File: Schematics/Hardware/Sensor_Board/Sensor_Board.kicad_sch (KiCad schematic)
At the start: 86 parts, among them J1 Conn_02x13_Odd_Even, J2 Conn_02x20_Odd_Even

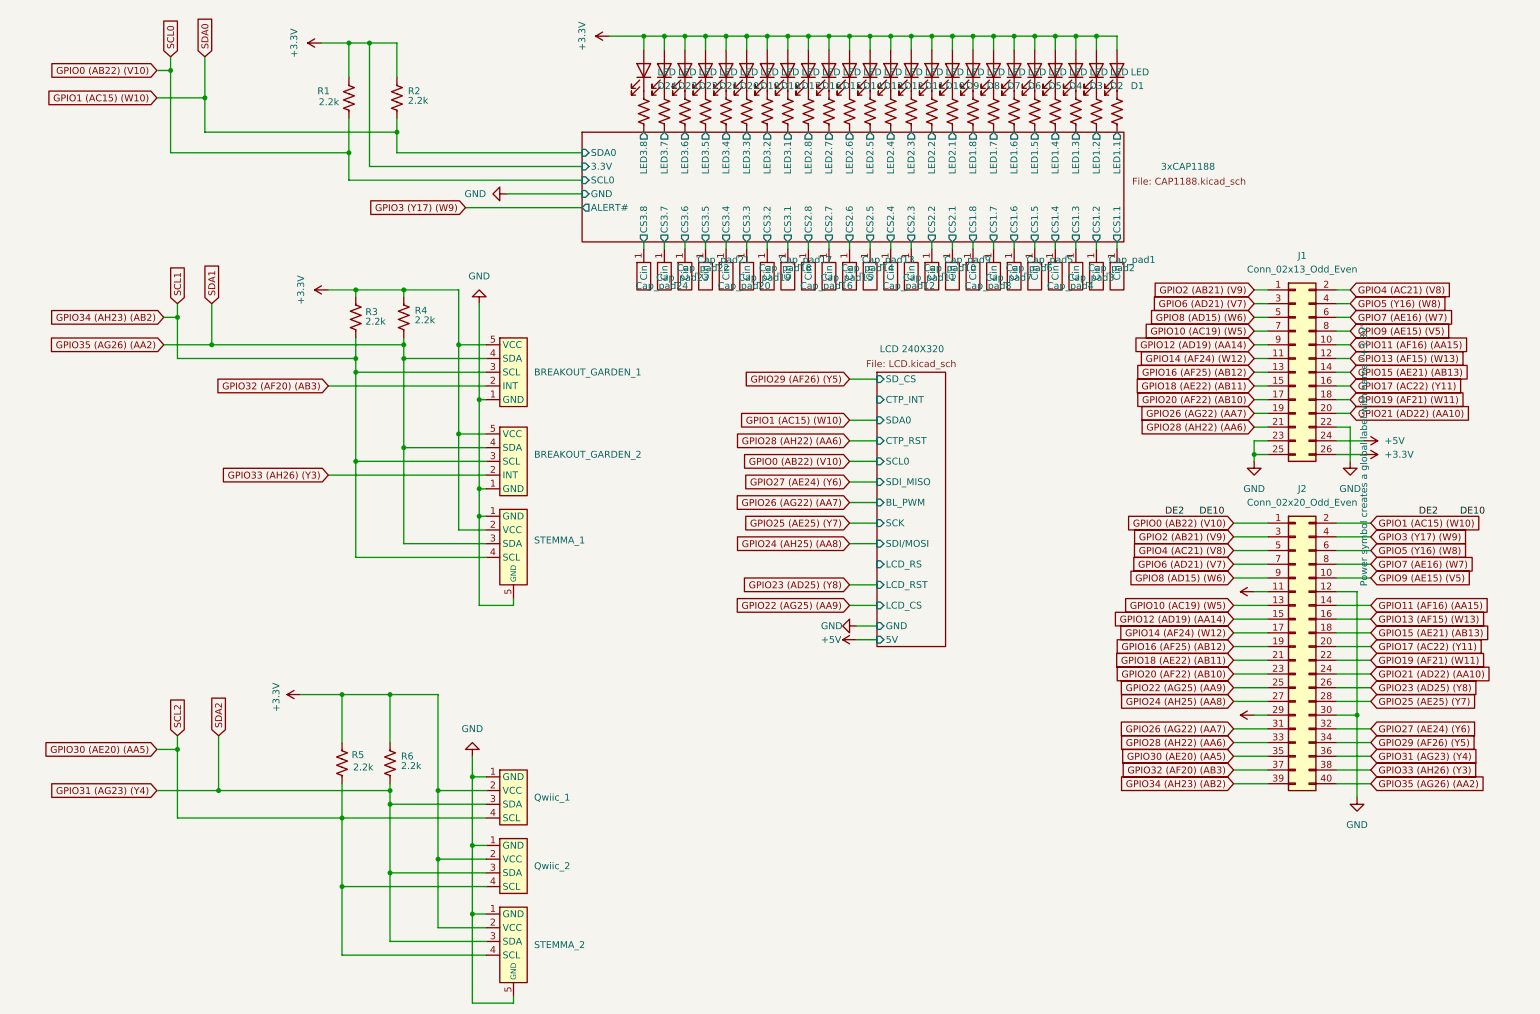
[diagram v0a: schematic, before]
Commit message: Updated Sensor board schematic/PCB
Still need to double check STEMMA connector and LCD standoff placement.
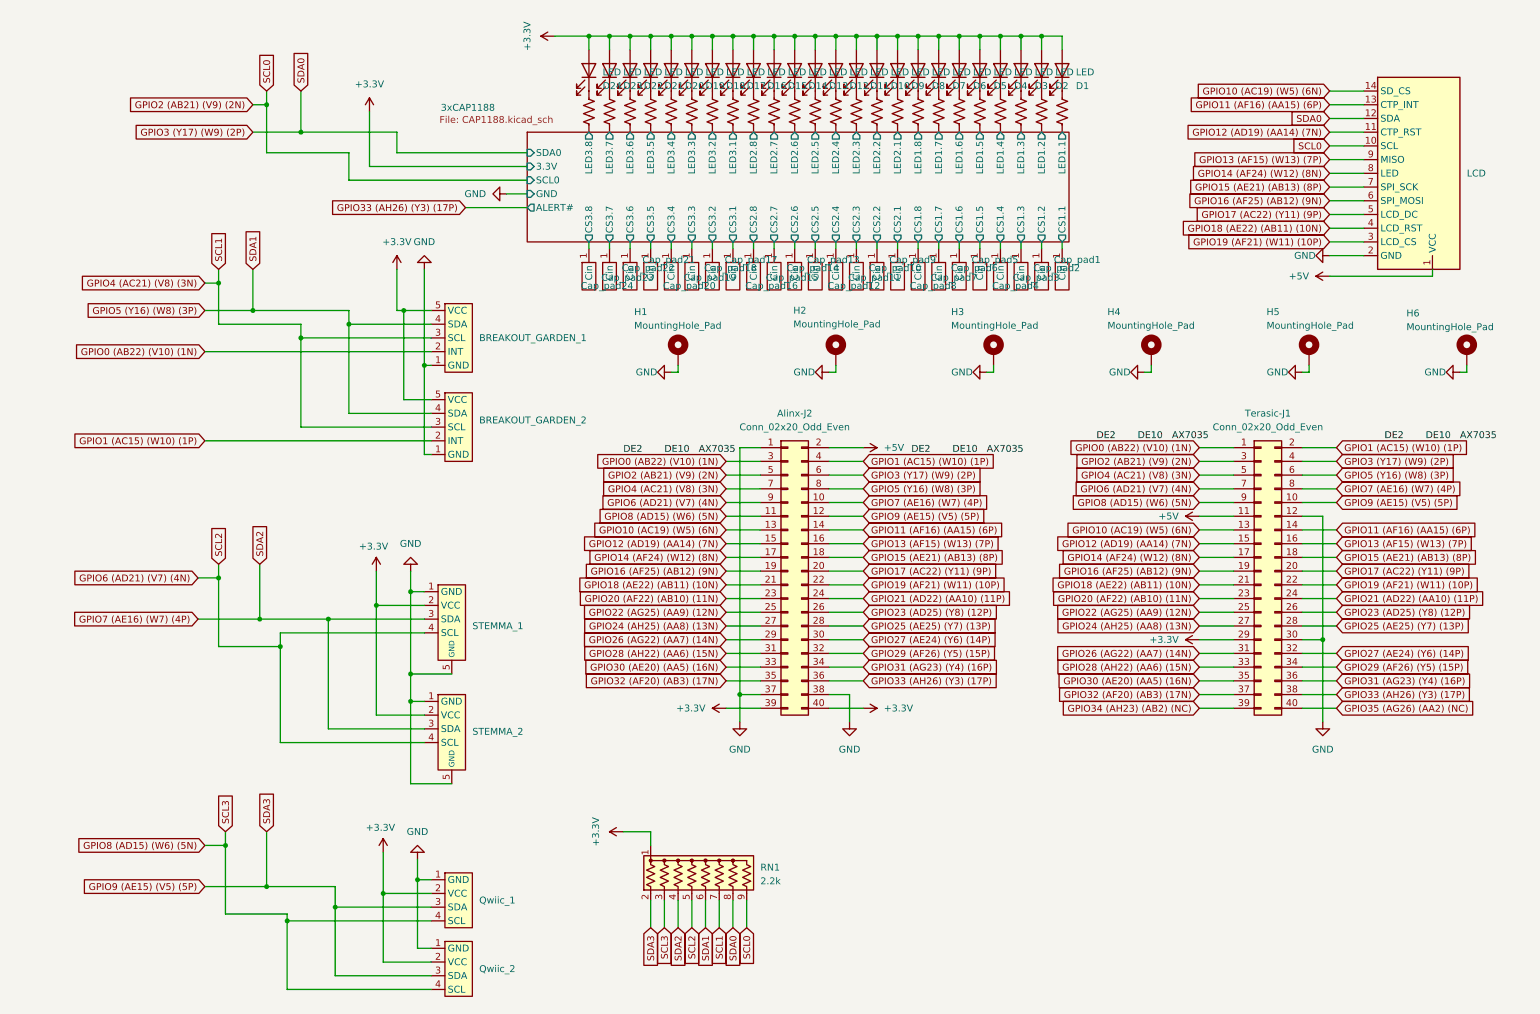
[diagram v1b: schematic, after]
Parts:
- removed J1: Conn_02x13_Odd_Even, Connector_PinHeader_2.54mm:PinHeader_2x13_P2.54mm_Vertical, symbol Connector_Generic:Conn_02x13_Odd_Even
- removed R1, R2, R3, R4, R5, R6: 2.2k, Resistor_THT:R_Axial_DIN0207_L6.3mm_D2.5mm_P10.16mm_Horizontal, symbol Device:R_US
- added Alinx-J2: Conn_02x20_Odd_Even, Connector_IDC:IDC-Header_2x20_P2.54mm_Vertical, symbol Connector_Generic:Conn_02x20_Odd_Even
- added H1, H2, H3, H4, H5, H6: MountingHole_Pad, MountingHole:MountingHole_2.5mm_Pad_Via, symbol Mechanical:MountingHole_Pad
- added RN1: 2.2k, Resistor_THT:R_Array_SIP9, symbol Device:R_Network08_US
- added U5: LCD, Connector_PinSocket_2.54mm:PinSocket_1x14_P2.54mm_Vertical, symbol Symbols:LCD240X320
- D1, D10, D11, D12, D13, D14, D15, D16, D17, D18, D19, D2, D20, D21, D22, D23, D24, D3, D4, D5, D6, D7, D8, D9: footprint LED_THT:LED_D3.0mm -> Diode_SMD:D_0805_2012Metric
- renumbered J2 to Terasic-J1
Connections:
- net GPIO4 (AC21) (V8) is gone; now on net GPIO4 (AC21) (V8) (3N): Terasic-J1.5 (Pin_5)
- net GPIO5 (Y16) (W8) is gone; now on net GPIO5 (Y16) (W8) (3P): Terasic-J1.6 (Pin_6)
- net GPIO8 (AD15) (W6) is gone; now on net GPIO8 (AD15) (W6) (5N): Terasic-J1.9 (Pin_9)
- net GPIO9 (AE15) (V5) is gone; now on net GPIO9 (AE15) (V5) (5P): Terasic-J1.10 (Pin_10)
- net +3.3V: now also Alinx-J2.39 (Pin_39), Alinx-J2.40 (Pin_40), RN1.1 (common)
- net +5V: now also Alinx-J2.2 (Pin_2), U5.1 (VCC)
- net GND: now also Alinx-J2.1 (Pin_1), Alinx-J2.37 (Pin_37), Alinx-J2.38 (Pin_38), H1.1, H2.1, H3.1, H4.1, H5.1, H6.1, U5.2 (VDD)
- net GPIO0 (AB22) (V10) renamed GPIO0 (AB22) (V10) (1N)
- net GPIO0 (AB22) (V10) (1N): now also BREAKOUT_GARDEN_1.2 (INT), Alinx-J2.3 (Pin_3)
- net GPIO1 (AC15) (W10) renamed GPIO1 (AC15) (W10) (1P)
- net GPIO1 (AC15) (W10) (1P): now also BREAKOUT_GARDEN_2.2 (INT), Alinx-J2.4 (Pin_4)
- net GPIO10 (AC19) (W5) renamed GPIO10 (AC19) (W5) (6N)
- net GPIO10 (AC19) (W5) (6N): now also Alinx-J2.13 (Pin_13), U5.14 (SD_CS)
- net GPIO11 (AF16) (AA15) renamed GPIO11 (AF16) (AA15) (6P)
- net GPIO11 (AF16) (AA15) (6P): now also Alinx-J2.14 (Pin_14), U5.13 (CTP_INT)
- net GPIO12 (AD19) (AA14) renamed GPIO12 (AD19) (AA14) (7N)
- net GPIO12 (AD19) (AA14) (7N): now also Alinx-J2.15 (Pin_15), U5.11 (CTP_RST)
- net GPIO13 (AF15) (W13) renamed GPIO13 (AF15) (W13) (7P)
- net GPIO13 (AF15) (W13) (7P): now also Alinx-J2.16 (Pin_16), U5.9 (MISO)
- net GPIO14 (AF24) (W12) renamed GPIO14 (AF24) (W12) (8N)
- net GPIO14 (AF24) (W12) (8N): now also Alinx-J2.17 (Pin_17), U5.8 (LED)
- net GPIO15 (AE21) (AB13) renamed GPIO15 (AE21) (AB13) (8P)
- net GPIO15 (AE21) (AB13) (8P): now also Alinx-J2.18 (Pin_18), U5.7 (SPI_SCK)
- net GPIO16 (AF25) (AB12) renamed GPIO16 (AF25) (AB12) (9N)
- net GPIO16 (AF25) (AB12) (9N): now also Alinx-J2.19 (Pin_19), U5.6 (SPI_MOSI)
- net GPIO17 (AC22) (Y11) renamed GPIO17 (AC22) (Y11) (9P)
- net GPIO17 (AC22) (Y11) (9P): now also Alinx-J2.20 (Pin_20), U5.5 (LCD_DC)
- net GPIO18 (AE22) (AB11) renamed GPIO18 (AE22) (AB11) (10N)
- net GPIO18 (AE22) (AB11) (10N): now also Alinx-J2.21 (Pin_21), U5.4 (LCD_RST)
- net GPIO19 (AF21) (W11) renamed GPIO19 (AF21) (W11) (10P)
- net GPIO19 (AF21) (W11) (10P): now also Alinx-J2.22 (Pin_22), U5.3 (VO)
- net GPIO2 (AB21) (V9) renamed GPIO2 (AB21) (V9) (2N)
- net GPIO2 (AB21) (V9) (2N): now also Alinx-J2.5 (Pin_5), RN1.9 (R8), U5.10 (SCL)
- net GPIO20 (AF22) (AB10) renamed GPIO20 (AF22) (AB10) (11N)
- net GPIO20 (AF22) (AB10) (11N): now also Alinx-J2.23 (Pin_23)
- net GPIO21 (AD22) (AA10) renamed GPIO21 (AD22) (AA10) (11P)
- net GPIO21 (AD22) (AA10) (11P): now also Alinx-J2.24 (Pin_24)
- net GPIO22 (AG25) (AA9) renamed GPIO22 (AG25) (AA9) (12N)
- net GPIO22 (AG25) (AA9) (12N): now also Alinx-J2.25 (Pin_25)
- net GPIO23 (AD25) (Y8) renamed GPIO23 (AD25) (Y8) (12P)
- net GPIO23 (AD25) (Y8) (12P): now also Alinx-J2.26 (Pin_26)
- net GPIO24 (AH25) (AA8) renamed GPIO24 (AH25) (AA8) (13N)
- net GPIO24 (AH25) (AA8) (13N): now also Alinx-J2.27 (Pin_27)
- net GPIO25 (AE25) (Y7) renamed GPIO25 (AE25) (Y7) (13P)
- net GPIO25 (AE25) (Y7) (13P): now also Alinx-J2.28 (Pin_28)
- net GPIO26 (AG22) (AA7) renamed GPIO26 (AG22) (AA7) (14N)
- net GPIO26 (AG22) (AA7) (14N): now also Alinx-J2.29 (Pin_29)
- net GPIO27 (AE24) (Y6) renamed GPIO27 (AE24) (Y6) (14P)
- net GPIO27 (AE24) (Y6) (14P): now also Alinx-J2.30 (Pin_30)
- net GPIO28 (AH22) (AA6) renamed GPIO28 (AH22) (AA6) (15N)
- net GPIO28 (AH22) (AA6) (15N): now also Alinx-J2.31 (Pin_31)
- net GPIO29 (AF26) (Y5) renamed GPIO29 (AF26) (Y5) (15P)
- net GPIO29 (AF26) (Y5) (15P): now also Alinx-J2.32 (Pin_32)
- net GPIO3 (Y17) (W9) renamed GPIO3 (Y17) (W9) (2P)
- net GPIO3 (Y17) (W9) (2P): now also Alinx-J2.6 (Pin_6), RN1.8 (R7), U5.12 (SDA)
- net GPIO30 (AE20) (AA5) renamed GPIO8 (AD15) (W6) (5N)
- net GPIO8 (AD15) (W6) (5N): now also Alinx-J2.11 (Pin_11), RN1.3 (R2); no longer STEMMA_2.4 (SCL), Terasic-J1.35 (Pin_35)
- net GPIO31 (AG23) (Y4) renamed GPIO9 (AE15) (V5) (5P)
- net GPIO9 (AE15) (V5) (5P): now also Alinx-J2.12 (Pin_12), RN1.2 (R1); no longer STEMMA_2.3 (SDA), Terasic-J1.36 (Pin_36)
- net GPIO32 (AF20) (AB3) renamed GPIO32 (AF20) (AB3) (17N)
- net GPIO32 (AF20) (AB3) (17N): now also Alinx-J2.35 (Pin_35); no longer BREAKOUT_GARDEN_1.2 (INT)
- net GPIO33 (AH26) (Y3) renamed GPIO33 (AH26) (Y3) (17P)
- net GPIO33 (AH26) (Y3) (17P): now also Alinx-J2.36 (Pin_36); no longer BREAKOUT_GARDEN_2.2 (INT)
- net GPIO34 (AH23) (AB2) renamed GPIO4 (AC21) (V8) (3N)
- net GPIO4 (AC21) (V8) (3N): now also Alinx-J2.7 (Pin_7), RN1.7 (R6); no longer STEMMA_1.4 (SCL), Terasic-J1.39 (Pin_39)
- net GPIO35 (AG26) (AA2) renamed GPIO5 (Y16) (W8) (3P)
- net GPIO5 (Y16) (W8) (3P): now also Alinx-J2.8 (Pin_8), RN1.6 (R5); no longer STEMMA_1.3 (SDA), Terasic-J1.40 (Pin_40)
- net GPIO6 (AD21) (V7) renamed GPIO6 (AD21) (V7) (4N)
- net GPIO6 (AD21) (V7) (4N): now also STEMMA_1.4 (SCL), STEMMA_2.4 (SCL), Alinx-J2.9 (Pin_9), RN1.5 (R4)
- net GPIO7 (AE16) (W7) renamed GPIO7 (AE16) (W7) (4P)
- net GPIO7 (AE16) (W7) (4P): now also STEMMA_1.3 (SDA), STEMMA_2.3 (SDA), Alinx-J2.10 (Pin_10), RN1.4 (R3)
- new net GPIO30 (AE20) (AA5) (16N): Alinx-J2.33 (Pin_33), Terasic-J1.35 (Pin_35)
- new net GPIO31 (AG23) (Y4) (16P): Alinx-J2.34 (Pin_34), Terasic-J1.36 (Pin_36)
- new net GPIO34 (AH23) (AB2) (NC): Terasic-J1.39 (Pin_39)
- new net GPIO35 (AG26) (AA2) (NC): Terasic-J1.40 (Pin_40)
- new net VDD: U5.2 (VDD)
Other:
- removed sheet LCD 240X320
- moved on the sheet: BREAKOUT_GARDEN_1, BREAKOUT_GARDEN_2, Cap_pad1, Cap_pad10, Cap_pad11, Cap_pad12, Cap_pad13, Cap_pad14, Cap_pad15, Cap_pad16, Cap_pad17, Cap_pad18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

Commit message: Added
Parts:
- removed U5: LCD, Connector_PinSocket_2.54mm:PinSocket_1x14_P2.54mm_Vertical, symbol Symbols:LCD240X320
- added H7, H8: MountingHole_Pad, MountingHole:MountingHole_2.5mm_Pad_Via, symbol Mechanical:MountingHole_Pad
- added J3: Conn_01x14, Connector_PinSocket_2.54mm:PinSocket_1x14_P2.54mm_Vertical, symbol Connector_Generic:Conn_01x14
- Qwiic_1, Qwiic_2: footprint Connector_JST:JST_SH_BM04B-SRSS-TB_1x04-1MP_P1.00mm_Vertical -> Connector_JST:JST_SH_SM04B-SRSS-TB_1x04-1MP_P1.00mm_Horizontal
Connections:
- net +5V: now also J3.1 (VCC)
- net GND: now also H7.1, H8.1, J3.2 (GND)
- net GPIO10 (AC19) (W5) (6N): now also J3.14 (SD_CS)
- net GPIO11 (AF16) (AA15) (6P): now also J3.13 (CTP_INT)
- net GPIO12 (AD19) (AA14) (7N): now also J3.11 (CTP_RST)
- net GPIO13 (AF15) (W13) (7P): now also J3.9 (SDO_MISO)
- net GPIO14 (AF24) (W12) (8N): now also J3.8 (LED)
- net GPIO15 (AE21) (AB13) (8P): now also J3.7 (SCK)
- net GPIO16 (AF25) (AB12) (9N): now also J3.6 (SDI_MOSI)
- net GPIO17 (AC22) (Y11) (9P): now also J3.5 (LCD_RS)
- net GPIO18 (AE22) (AB11) (10N): now also J3.4 (LCD_RST)
- net GPIO19 (AF21) (W11) (10P): now also J3.3 (LCD_CS)
- net GPIO2 (AB21) (V9) (2N): now also J3.10 (CTP_SCL)
- net GPIO3 (Y17) (W9) (2P): now also J3.12 (CTP_SDA)
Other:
- moved on the sheet: H2, H3, H4, H5, H6
